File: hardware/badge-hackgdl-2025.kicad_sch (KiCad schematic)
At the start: 20 parts, among them P1 USB_C_Plug_USB2.0, Q1 DMG3415U-7, SW1 ON, SW2 RESET, SW3 BOOT, U1 XC6220B331MR-G, U2 ESP32-S3-WROOM-1-N16

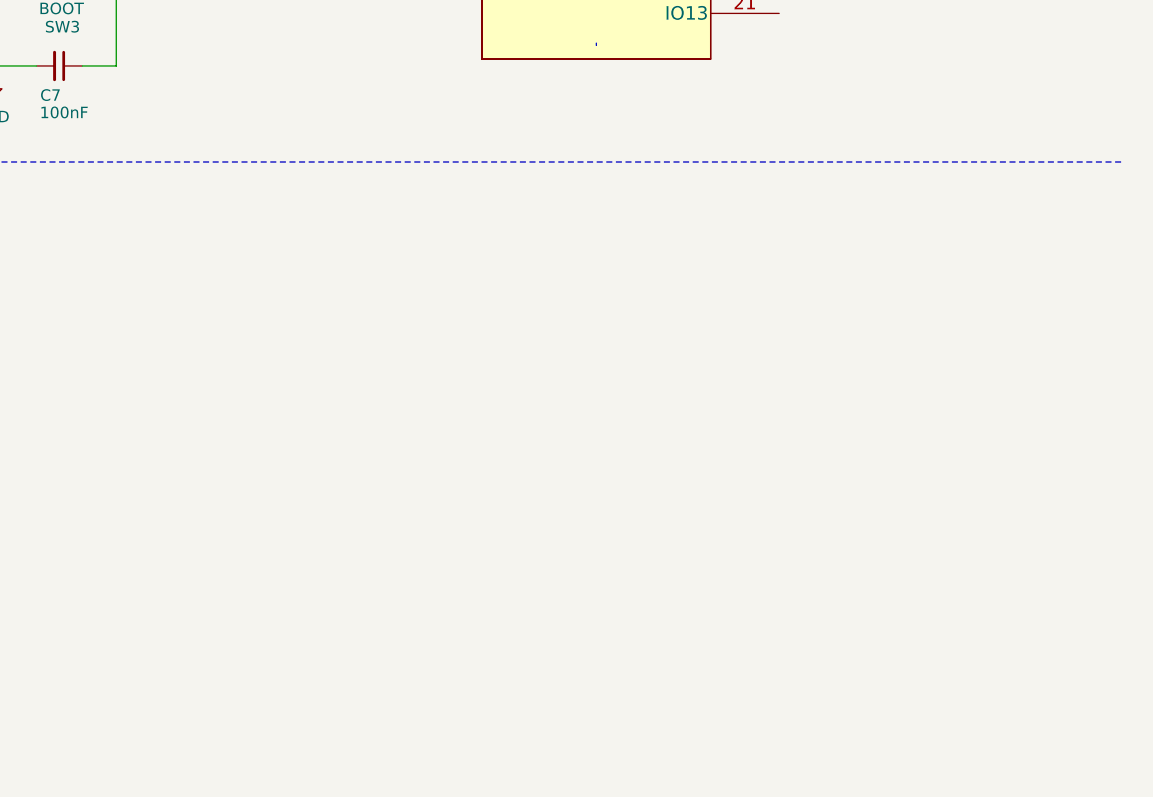
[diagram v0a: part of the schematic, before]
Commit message: feat(hw): add neopixels in the schematic
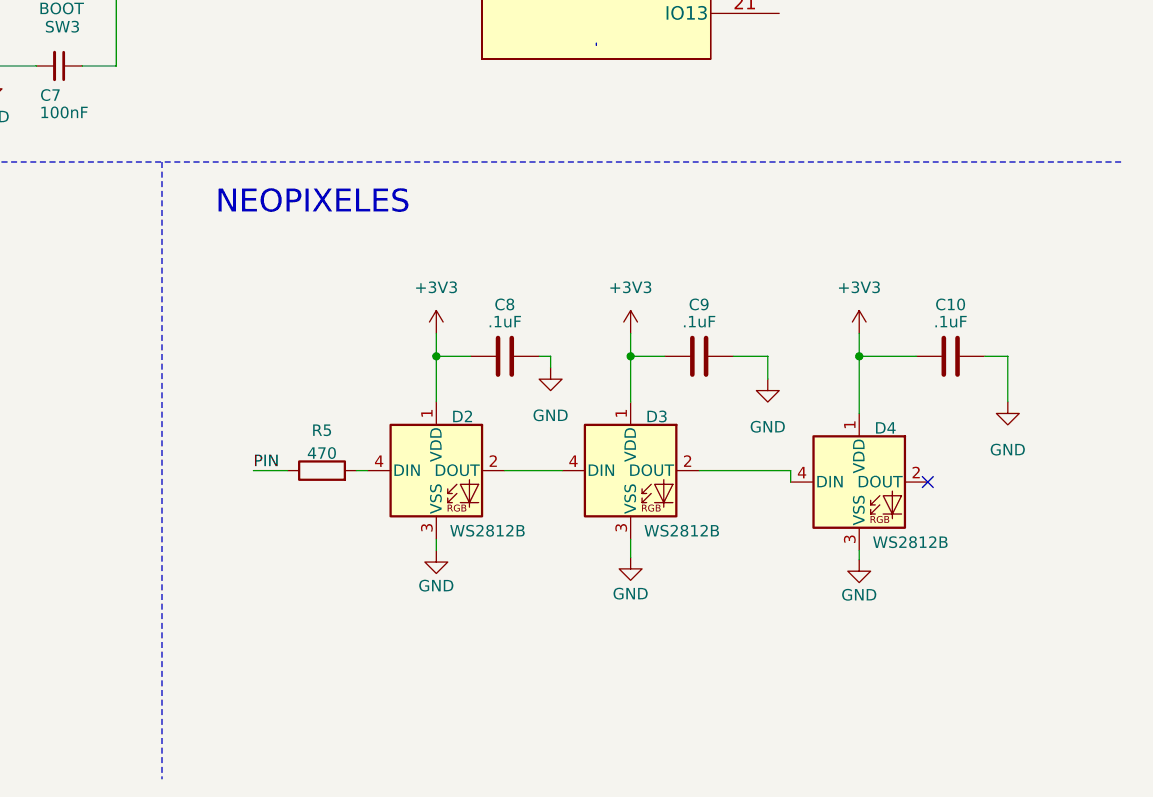
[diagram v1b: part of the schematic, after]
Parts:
- added C10, C8, C9: .1uF, Capacitor_SMD:C_0603_1608Metric, symbol Device:C
- added D2, D3, D4: WS2812B, LED_SMD:LED_WS2812B-Mini_PLCC4_3.5x3.5mm, symbol LED:WS2812B
- added R5: 470, Resistor_SMD:R_0603_1608Metric, symbol Device:R
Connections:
- net +3V3: now also C10.2, C8.2, C9.2, D2.1 (VDD), D3.1 (VDD), D4.1 (VDD)
- net GND: now also C10.1, C8.1, C9.1, D2.3 (VSS), D3.3 (VSS), D4.3 (VSS)
- new net: D3.2 (DOUT), D4.4 (DIN)
- new net: D2.2 (DOUT), D3.4 (DIN)
- new net: D2.4 (DIN), R5.2
- new net PIN: R5.1
- no-connect marks 7 -> 8
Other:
- note added: "NEOPIXELES"

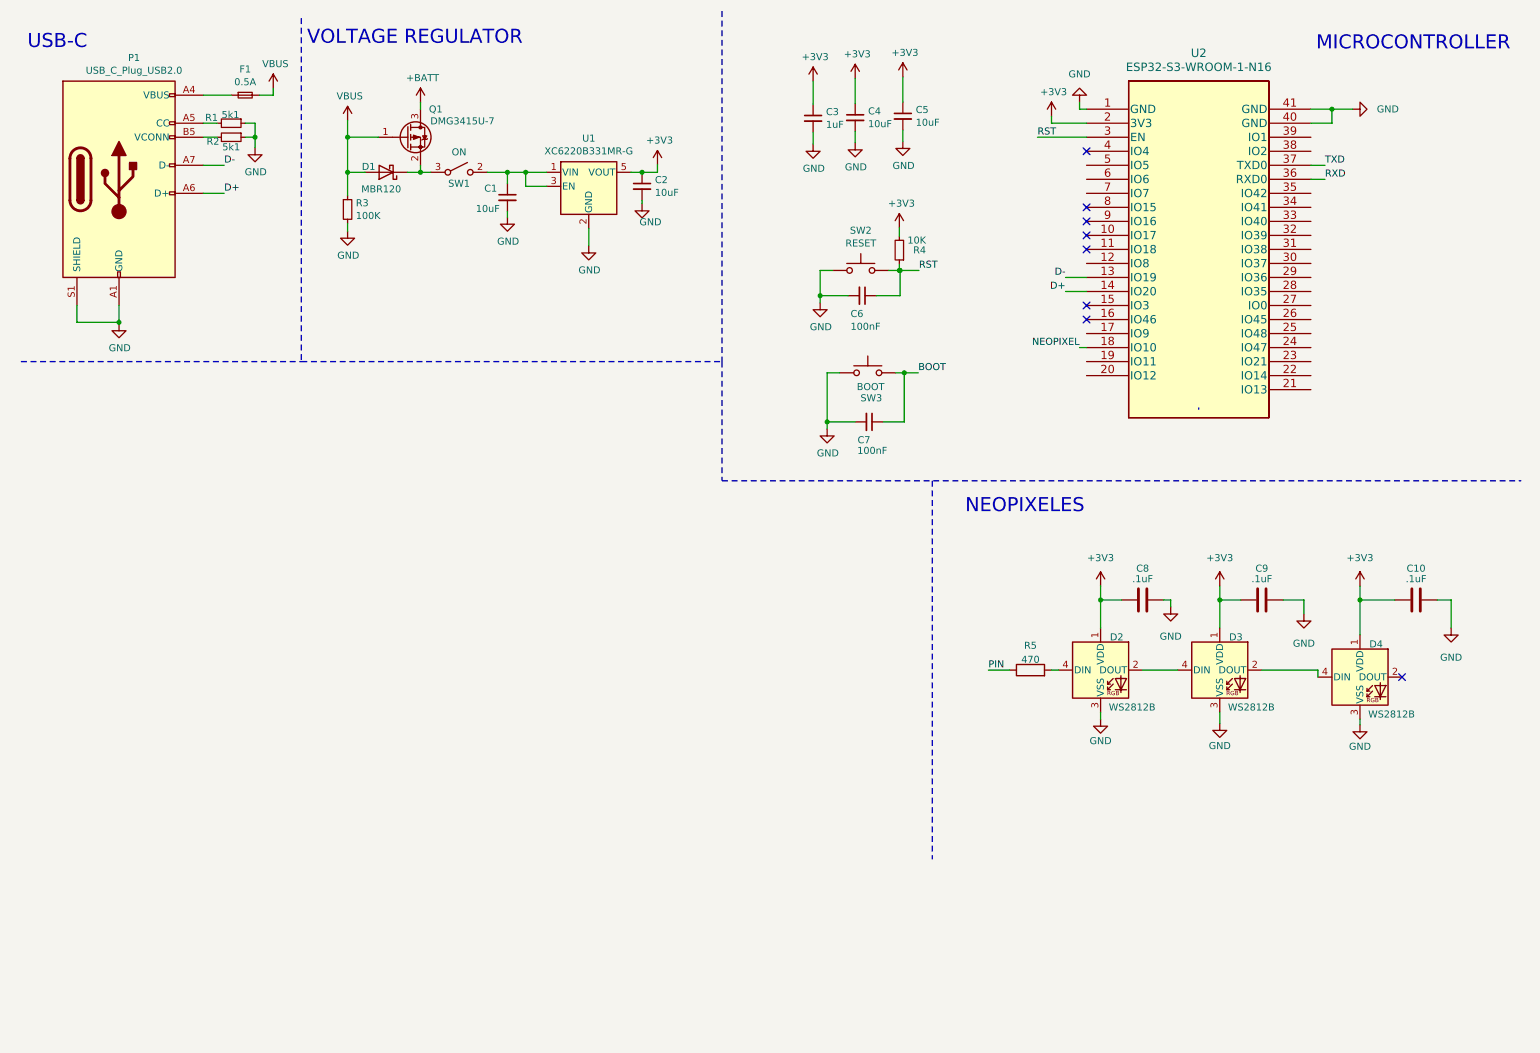
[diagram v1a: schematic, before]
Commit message: feat(hw): add buttons and buzzer
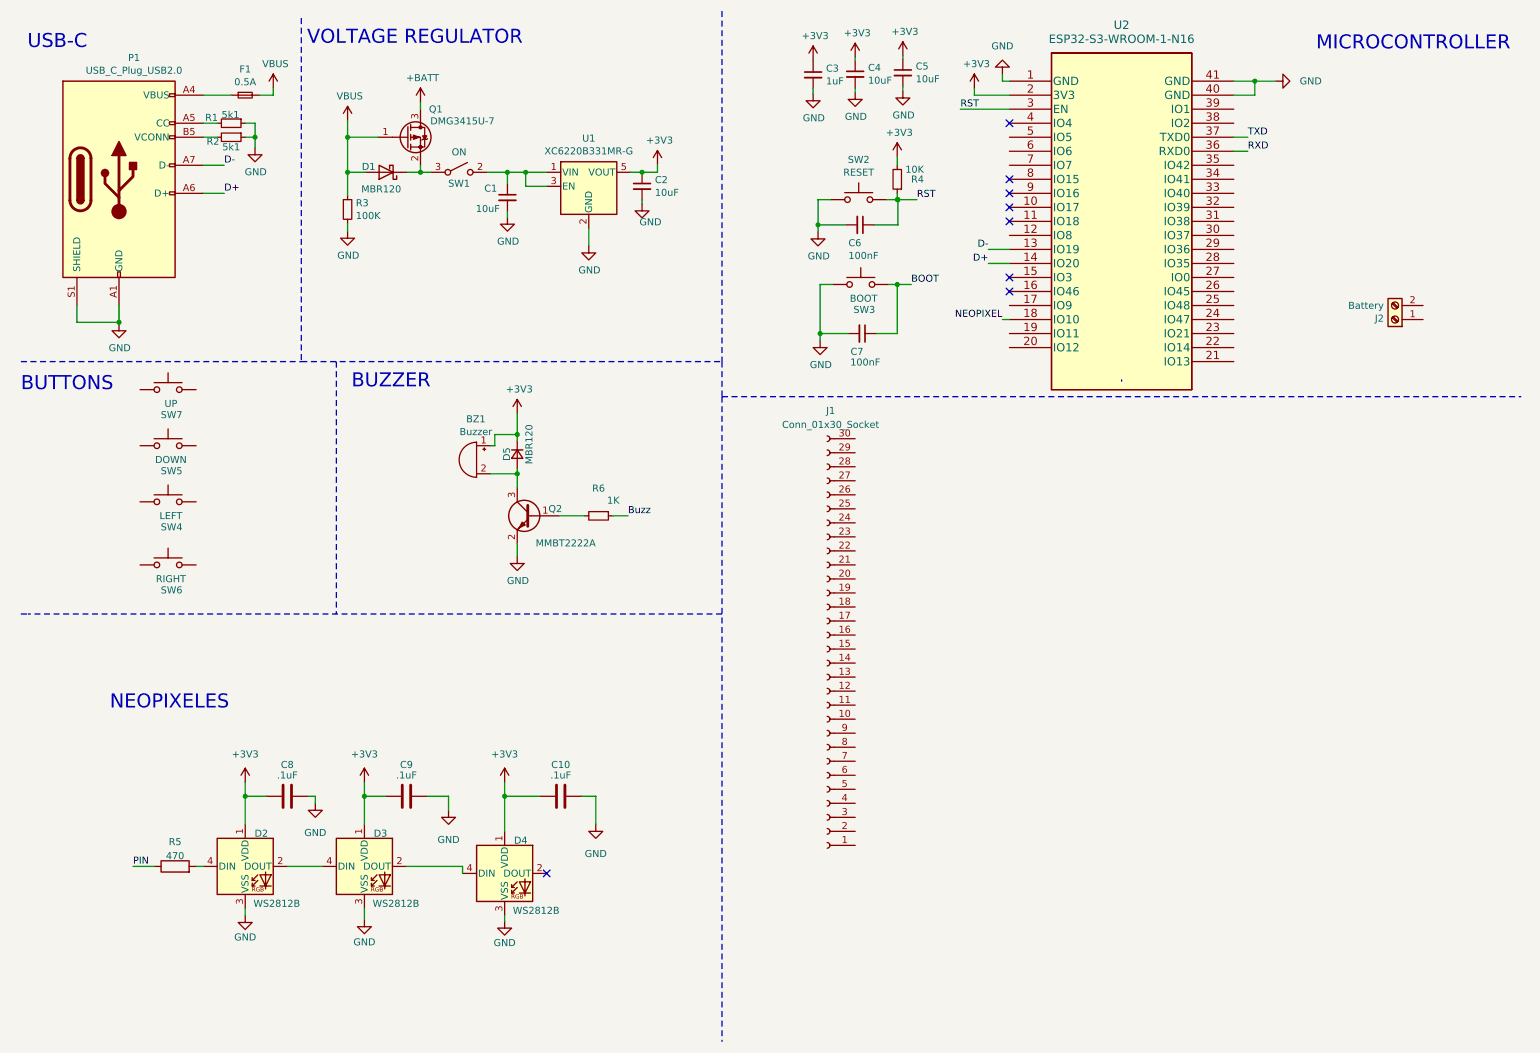
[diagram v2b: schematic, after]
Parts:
- added BZ1: Buzzer, Footprint:Buzzer4x4, symbol Device:Buzzer
- added D5: MBR120, Diode_SMD:D_SOD-123F, symbol Device:D_Small
- added J1: Conn_01x30_Socket, symbol Connector:Conn_01x30_Socket
- added J2: Battery, Footprints:BAT-TH_BH-AAA-A1AJ024, symbol Connector:Screw_Terminal_01x02
- added Q2: MMBT2222A, Package_TO_SOT_SMD:SOT-23, symbol Transistor_BJT:PN2222A
- added R6: 1K, Resistor_SMD:R_0603_1608Metric_Pad0.98x0.95mm_HandSolder, symbol Device:R_Small
- added SW4: LEFT, Button_Switch_SMD:SW_Push_SPST_NO_Alps_SKRK, symbol Switch:SW_Push
- added SW5: DOWN, Button_Switch_SMD:SW_Push_SPST_NO_Alps_SKRK, symbol Switch:SW_Push
- added SW6: RIGHT, Button_Switch_SMD:SW_Push_SPST_NO_Alps_SKRK, symbol Switch:SW_Push
- added SW7: UP, Button_Switch_SMD:SW_Push_SPST_NO_Alps_SKRK, symbol Switch:SW_Push
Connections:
- net +3V3: now also BZ1.1 (-), D5.1 (K)
- net GND: now also Q2.2 (E)
- new net: Q2.1 (B), R6.2
- new net: BZ1.2 (+), D5.2 (A), Q2.3 (C)
- new net Buzz: R6.1
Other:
- note added: "BUTTONS"
- note added: "BUZZER"
- moved on the sheet: C10, C3, C4, C5, C6, C7, C8, C9, D2, D3, D4, R4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

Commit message: feat: add oled connector
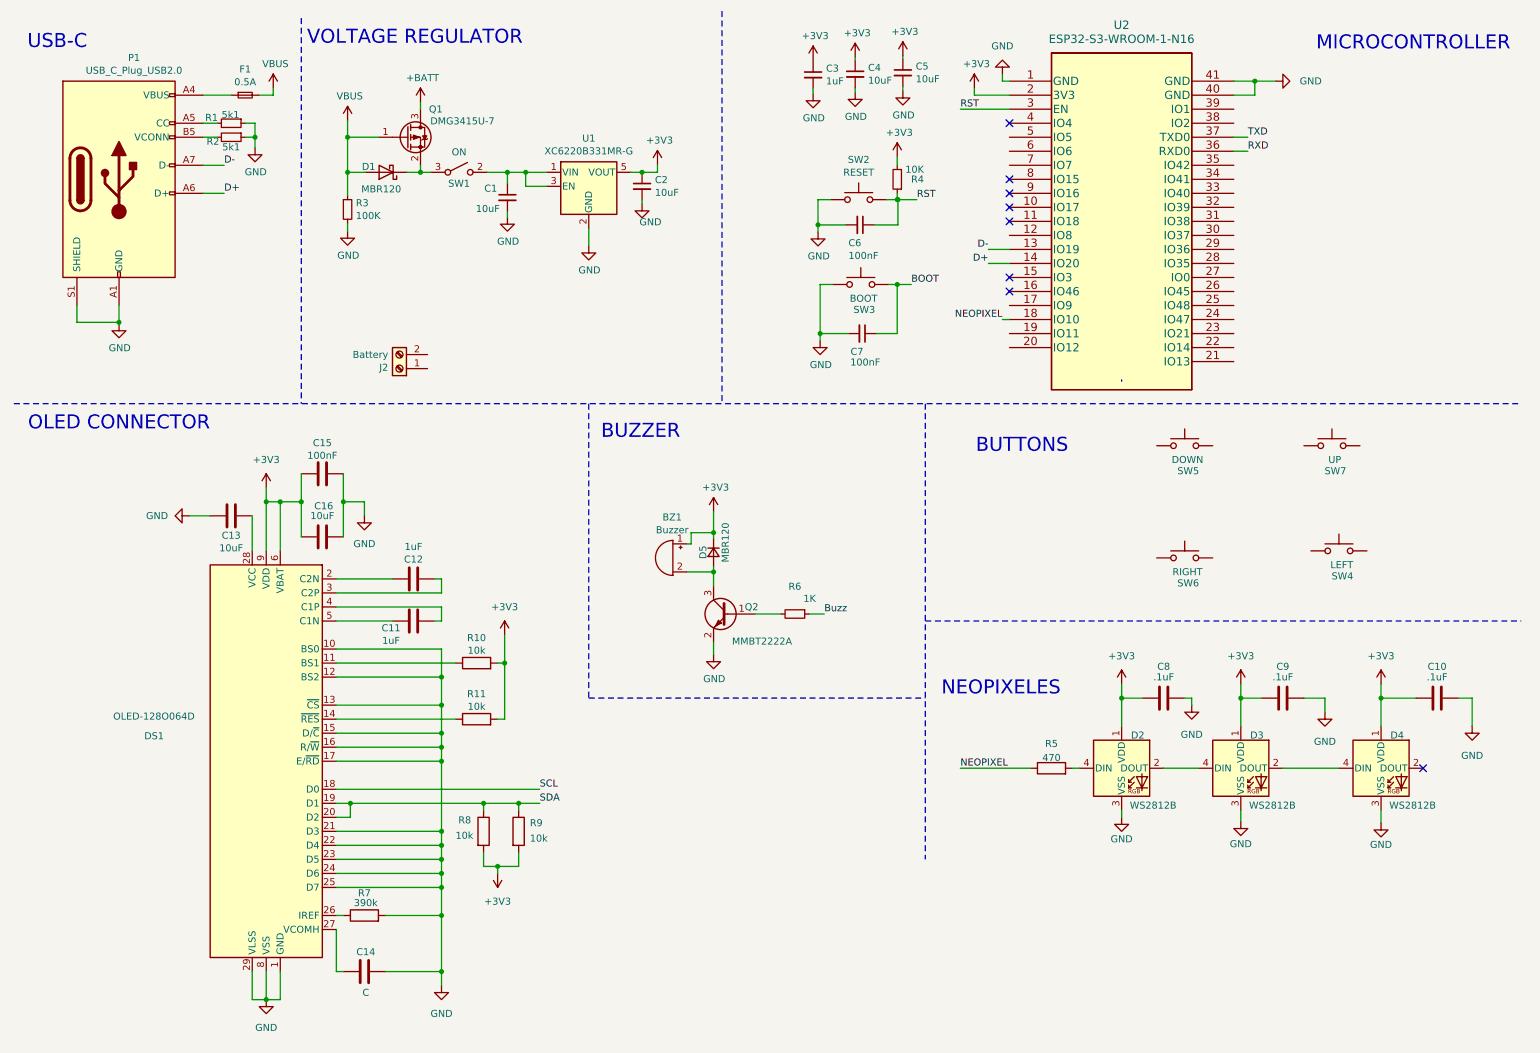
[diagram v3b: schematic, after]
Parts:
- removed J1: Conn_01x30_Socket, symbol Connector:Conn_01x30_Socket
- added C11, C12: 1uF, symbol Device:C
- added C13, C16: 10uF, symbol Device:C
- added C14: C, symbol Device:C
- added C15: 100nF, symbol Device:C
- added DS1: OLED-128O064D, Display:OLED-128O064D, symbol Display_Graphic:OLED-128O064D
- added R10, R11, R8, R9: 10k, symbol Device:R
- added R7: 390k, symbol Device:R
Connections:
- net PIN is gone; now on net NEOPIXEL: R5.1
- net +3V3: now also C15.1, C16.1, DS1.6 (VBAT), DS1.9 (VDD), R10.2, R11.2, R8.2, R9.2
- net GND: now also C13.1, C14.2, C15.2, C16.2, DS1.1 (GND), DS1.10 (BS0), DS1.12 (BS2), DS1.13 (~{CS}), DS1.15 (D/~{C}), DS1.16 (R/~{W}), DS1.17 (E/~{RD}), DS1.21 (D3), DS1.22 (D4), DS1.23 (D5), DS1.24 (D6), DS1.25 (D7), DS1.29 (VLSS), DS1.30 (GND), DS1.8 (VSS), R7.2
- new net: C14.1, DS1.27 (VCOMH)
- new net: DS1.11 (BS1), R10.1
- new net: DS1.14 (~{RES}), R11.1
- new net: C12.2, DS1.2 (C2N)
- new net: DS1.26 (IREF), R7.1
- new net: C13.2, DS1.28 (VCC)
- new net: C12.1, DS1.3 (C2P)
- new net: C11.2, DS1.4 (C1P)
- new net: C11.1, DS1.5 (C1N)
- new net SCL: DS1.18 (D0)
- new net SDA: DS1.19 (D1), DS1.20 (D2), R8.1, R9.1
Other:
- note added: "OLED CONNECTOR"
- moved on the sheet: BZ1, C10, C8, C9, D2, D3, D4, D5, J2, Q2, R5, R6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

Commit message: feat: add components in schematic
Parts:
- added C17, C18, C19, C20: 100nF, Capacitor_SMD:C_0603_1608Metric, symbol Device:C_Small
- added J1: ADDON, Connector_PinSocket_2.54mm:PinSocket_2x03_P2.54mm_Vertical_SMD, symbol Connector_Generic:Conn_02x03_Odd_Even
- BZ1: footprint Footprint:Buzzer4x4 -> Footprints:Buzzer4x4
- C1, C2: Proveedor (none) -> JLCPCB; manf# (none) -> GRM188R61E106KA73J
- C11, C12, C13, C15, C16: footprint (none) -> Capacitor_SMD:C_0603_1608Metric
- C14: value C -> 10uF; footprint (none) -> Capacitor_SMD:C_0603_1608Metric
- D1: Proveedor (none) -> JLCPCB; manf# MBR120LSF -> MBR120LSFT1G
- Q1: Proveedor (none) -> JLCPCB; manf# DMG3415U-7 -> DMG3415UQ-7
- R10, R11, R7, R8, R9: footprint (none) -> Resistor_SMD:R_0603_1608Metric
- R3: Proveedor LCSC -> JLCPCB; manf# (none) -> RC0603DR-07100KL
- R6: footprint Resistor_SMD:R_0603_1608Metric_Pad0.98x0.95mm_HandSolder -> Resistor_SMD:R_0603_1608Metric
- SW1: LCSC# C221660 -> C431540; Proveedor (none) -> JLCPCB; manf# JS102011SAQN -> (none)
- SW4, SW6: footprint Button_Switch_SMD:SW_Push_SPST_NO_Alps_SKRK -> Button_Switch_SMD:SW_SPST_TL3342
- SW5: value DOWN -> BACK; footprint Button_Switch_SMD:SW_Push_SPST_NO_Alps_SKRK -> Button_Switch_SMD:SW_SPST_TL3342
- SW7: value UP -> MIDDLE; footprint Button_Switch_SMD:SW_Push_SPST_NO_Alps_SKRK -> Button_Switch_SMD:SW_SPST_TL3342
- U1: Proveedor (none) -> JLCPCB
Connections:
- net +3V3: now also SW1.3 (A), J1.1 (Pin_1); no longer C2.1, U1.5 (VOUT)
- net +BATT: now also J2.2 (Pin_2)
- net BOOT: now also U2.27 (IO0)
- net Buzz: now also U2.21 (IO13)
- net GND: now also J2.1 (Pin_1), SW4.1, SW5.1, SW6.1, SW7.1, C17.2, C18.2, C19.2, C20.2, J1.2 (Pin_2)
- net SCL: now also R9.1, U2.17 (IO9), J1.4 (Pin_4)
- net SDA: now also U2.12 (IO8), J1.3 (Pin_3); no longer R9.1
- net VBUS: now also C1.1, U1.1 (VIN), U1.3 (EN); no longer D1.2 (A), Q1.1 (G), R3.1
- net MIDDLE: now reaches SW7.2
- net MIDDLE: now also U2.8 (IO15), C17.1
- net at D1.1 (K), Q1.2 (S): now also SW1.2 (B); no longer SW1.3 (A)
- net LEFT: now reaches SW4.2
- net LEFT: now also U2.10 (IO17), C20.1
- net BACK: now reaches SW5.2
- net BACK: now also U2.11 (IO18), C18.1
- net RIGHT: now reaches SW6.2
- net RIGHT: now also U2.9 (IO16), C19.1
- new net: C2.1, D1.2 (A), Q1.1 (G), R3.1, U1.5 (VOUT)
- no-connect marks 8 -> 26
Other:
- note added: "SHITTY-ADDON"
- moved on the sheet: C11, C12, C13, C14, C15, C16, DS1, R10, R11, R7, R8, R9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

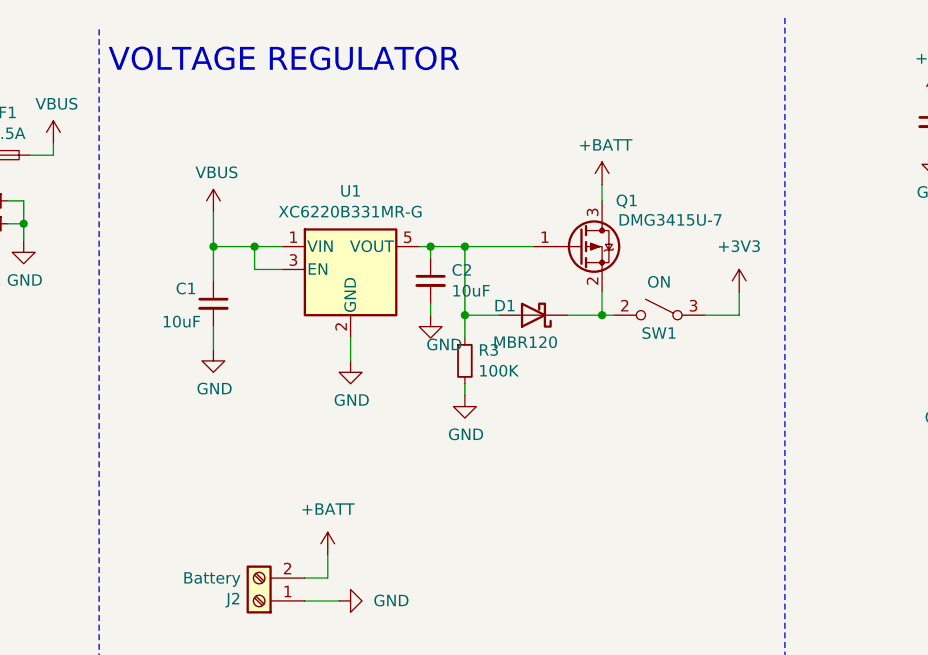
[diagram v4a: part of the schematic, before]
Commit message: feat(hw): add floor plan
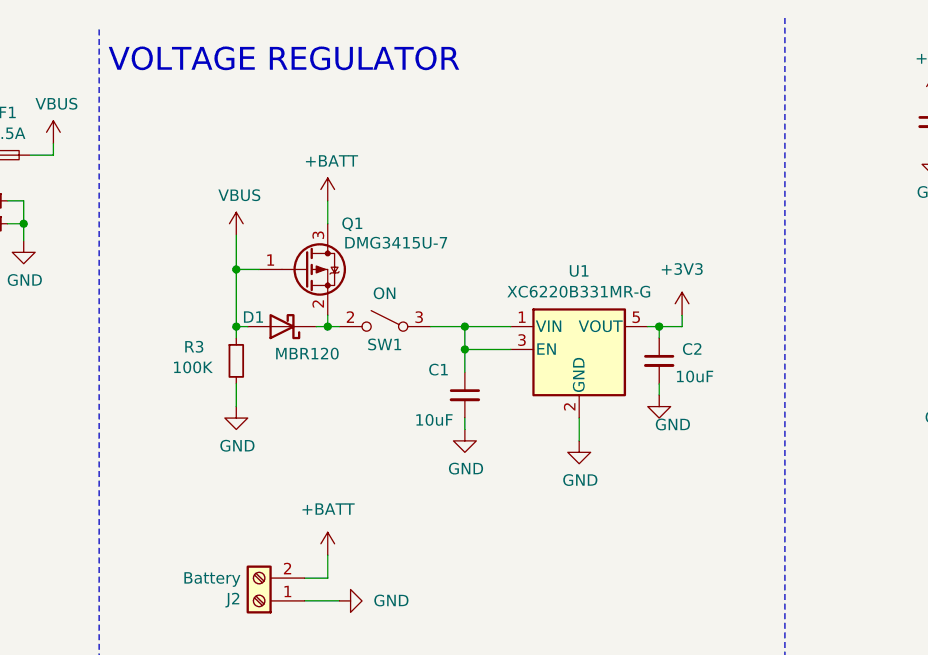
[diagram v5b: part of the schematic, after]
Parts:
- DS1: footprint Display:OLED-128O064D -> Footprints:ssd1306_oled_conn
- SW2, SW3: footprint Button_Switch_SMD:SW_Push_SPST_NO_Alps_SKRK -> Button_Switch_SMD:SW_SPST_TL3342
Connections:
- net +3V3: now also C2.1, U1.5 (VOUT); no longer SW1.3 (A)
- net VBUS: now also D1.2 (A), Q1.1 (G), R3.1; no longer C1.1, U1.1 (VIN), U1.3 (EN)
- new net: C1.1, SW1.3 (A), U1.1 (VIN), U1.3 (EN)
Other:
- moved on the sheet: C1, C2, D1, Q1, R3, SW1, U1
